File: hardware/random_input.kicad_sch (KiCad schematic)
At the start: 18 parts, among them J1 E1, J2 E2, Q1 NPN Ge, Q2 NPN Ge

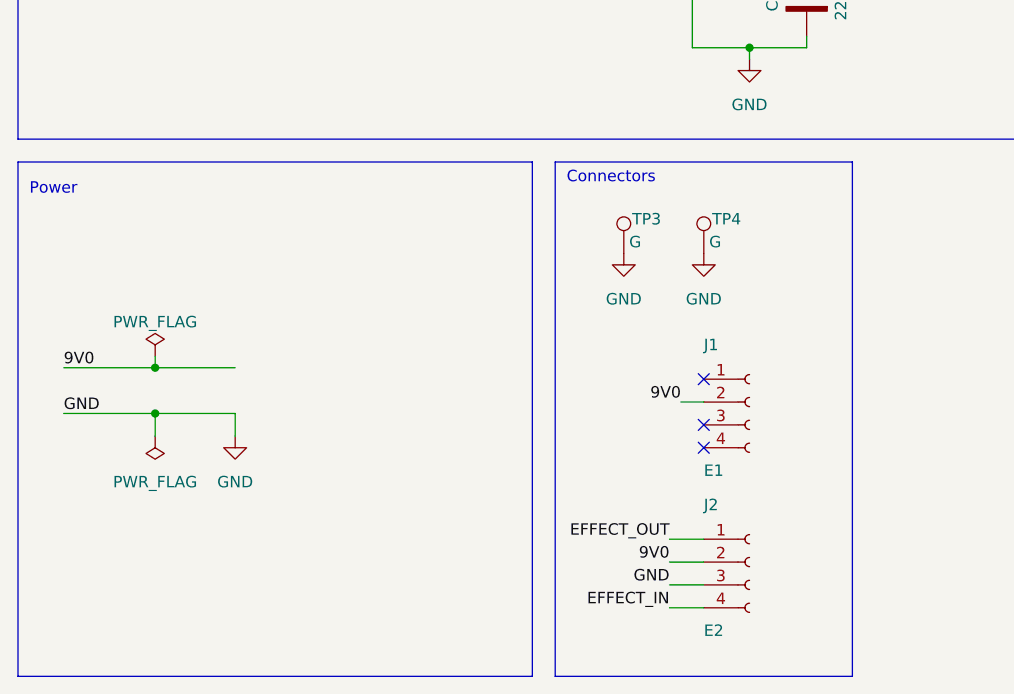
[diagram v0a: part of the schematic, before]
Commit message: Drop to a single connector to simplify, bump rev to v0.26
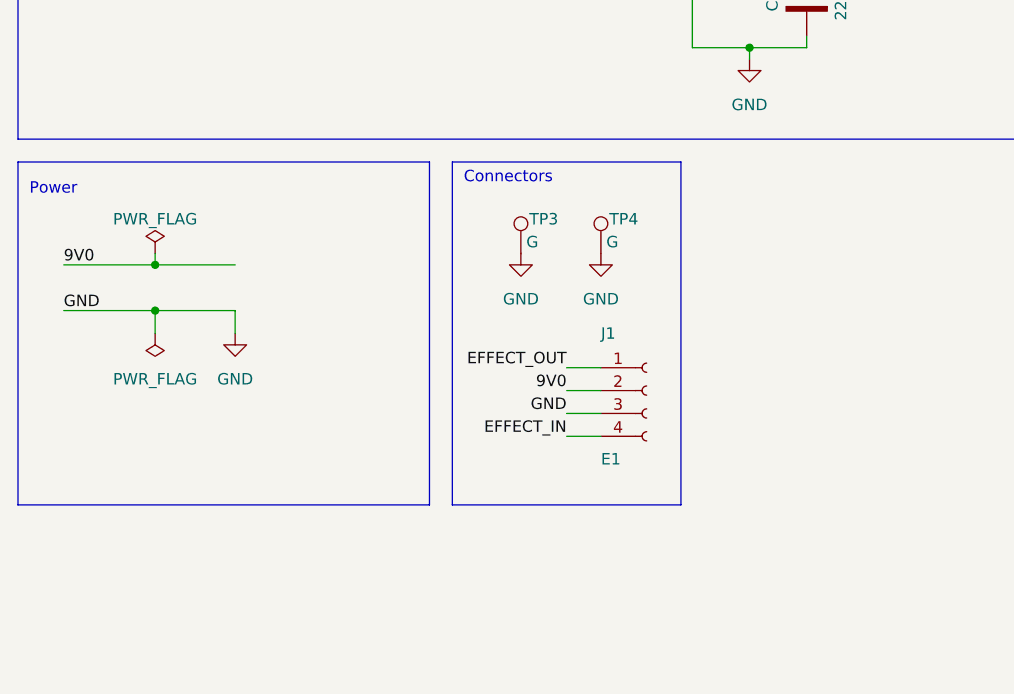
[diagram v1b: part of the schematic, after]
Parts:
- removed J1: E1, Connector_Molex:Molex_PicoBlade_53047-0410_1x04_P1.25mm_Vertical, symbol Connector:Conn_01x04_Socket
- J1: renamed from J2; value E2 -> E1
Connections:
- no-connect marks 3 -> 0
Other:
- moved on the sheet: J1, TP3, TP4

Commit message: Some updates based on feedback from freestompboxes.org folks:
 - Add back thermal reliefs on ground pads
 - Add 3D models for various parts (courtesy of Vasily Kashirin - https://grabcad.com/vasily.kashirin-1/models?page=1)
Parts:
- J1: footprint Connector_Molex:Molex_PicoBlade_53047-0410_1x04_P1.25mm_Vertical -> random_input:Molex_PicoBlade_53047-0410_1x04_P1.25mm_Vertical_with_3D_Model
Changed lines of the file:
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@@
   (title_block
     (title "Random Input Fuzz Effect (Based on Fuzz Face)")
-    (date "2023-03-03")
-    (rev "v0.26")
+    (date "2023-03-04")
+    (rev "v0.27")
   )
   (junction (at 29.21 114.3) (diameter 0) (color 0 0 0 0)
@@
       (effects (font (size 1.27 1.27)) (justify left))
     )
-    (property "Footprint" "Connector_Molex:Molex_PicoBlade_53047-0410_1x04_P1.25mm_Vertical" (at 83.82 123.19 0)
-      (effects (font (size 1.27 1.27)) hide)
-    )
+    (property "Footprint" "random_input:Molex_PicoBlade_53047-0410_1x04_P1.25mm_Vertical_with_3D_Model" (at 83.82 123.19 0)
+      (effects (font (size 1.27 1.27)) hide)
+    )
